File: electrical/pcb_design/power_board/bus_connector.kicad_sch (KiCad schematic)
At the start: 7 parts, among them J601 Interconnect_Power_CPU-Power_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, J603 Interconnect_Battery_Power-Po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

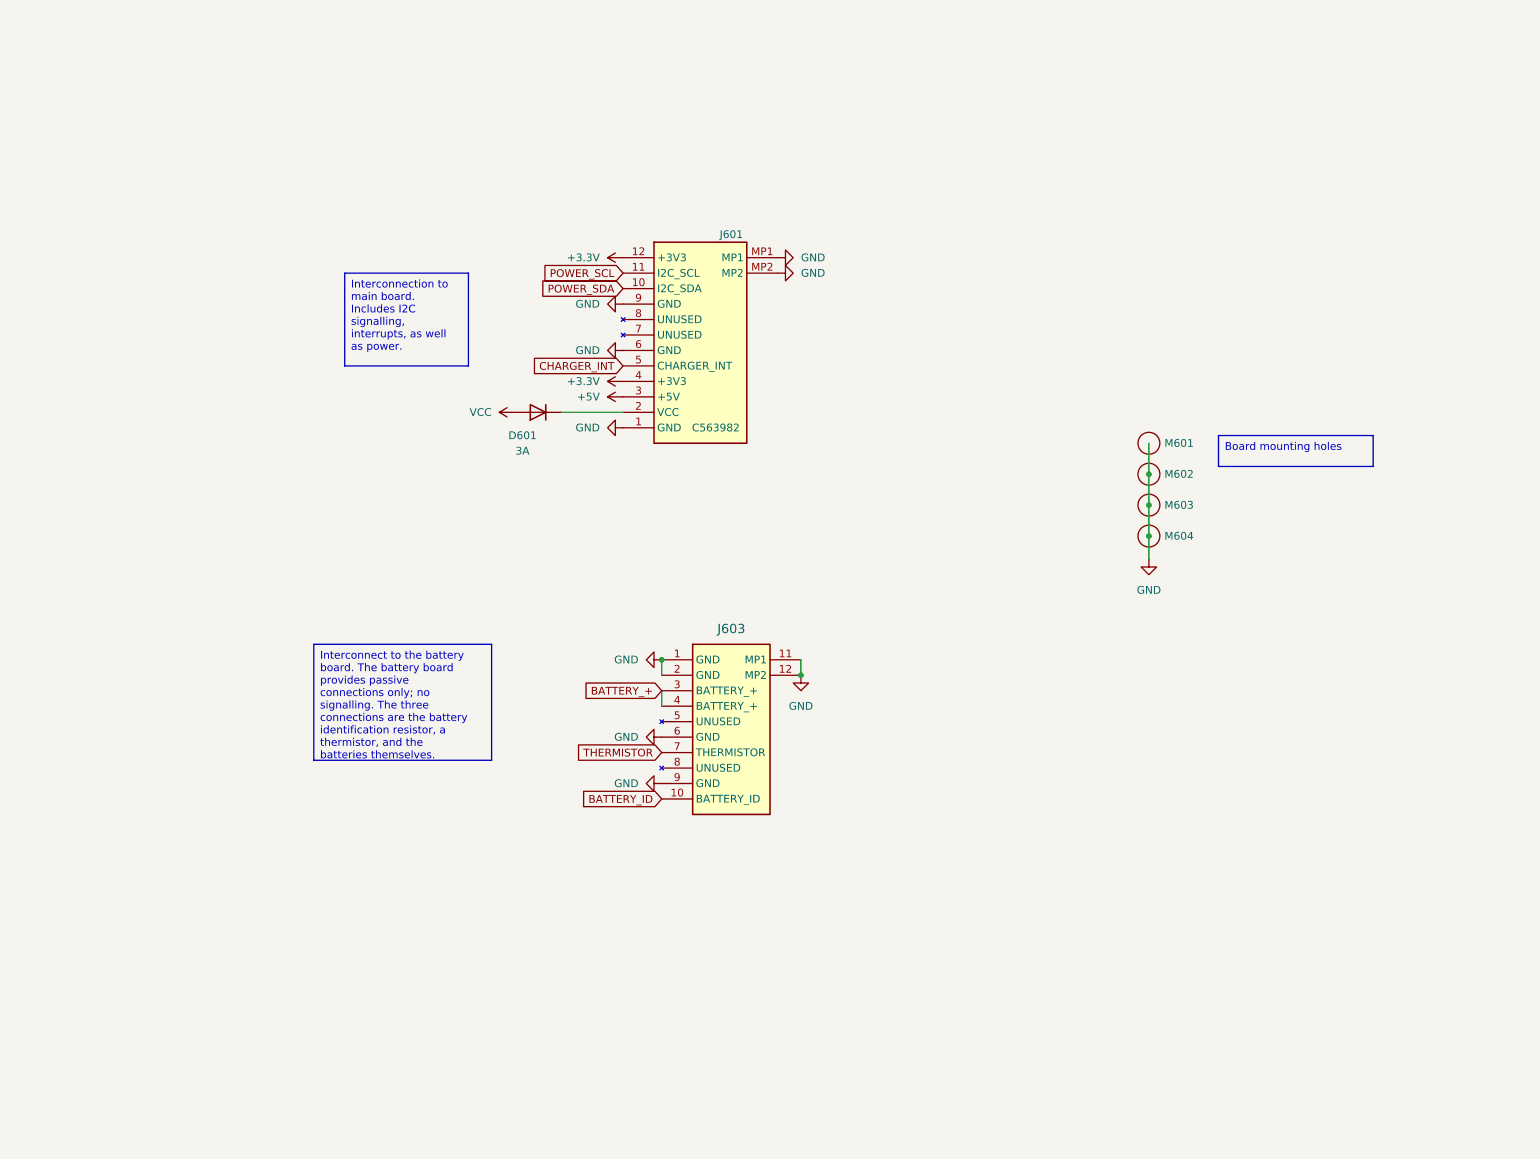
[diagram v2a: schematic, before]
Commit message: Sketched in PCB edge connectors
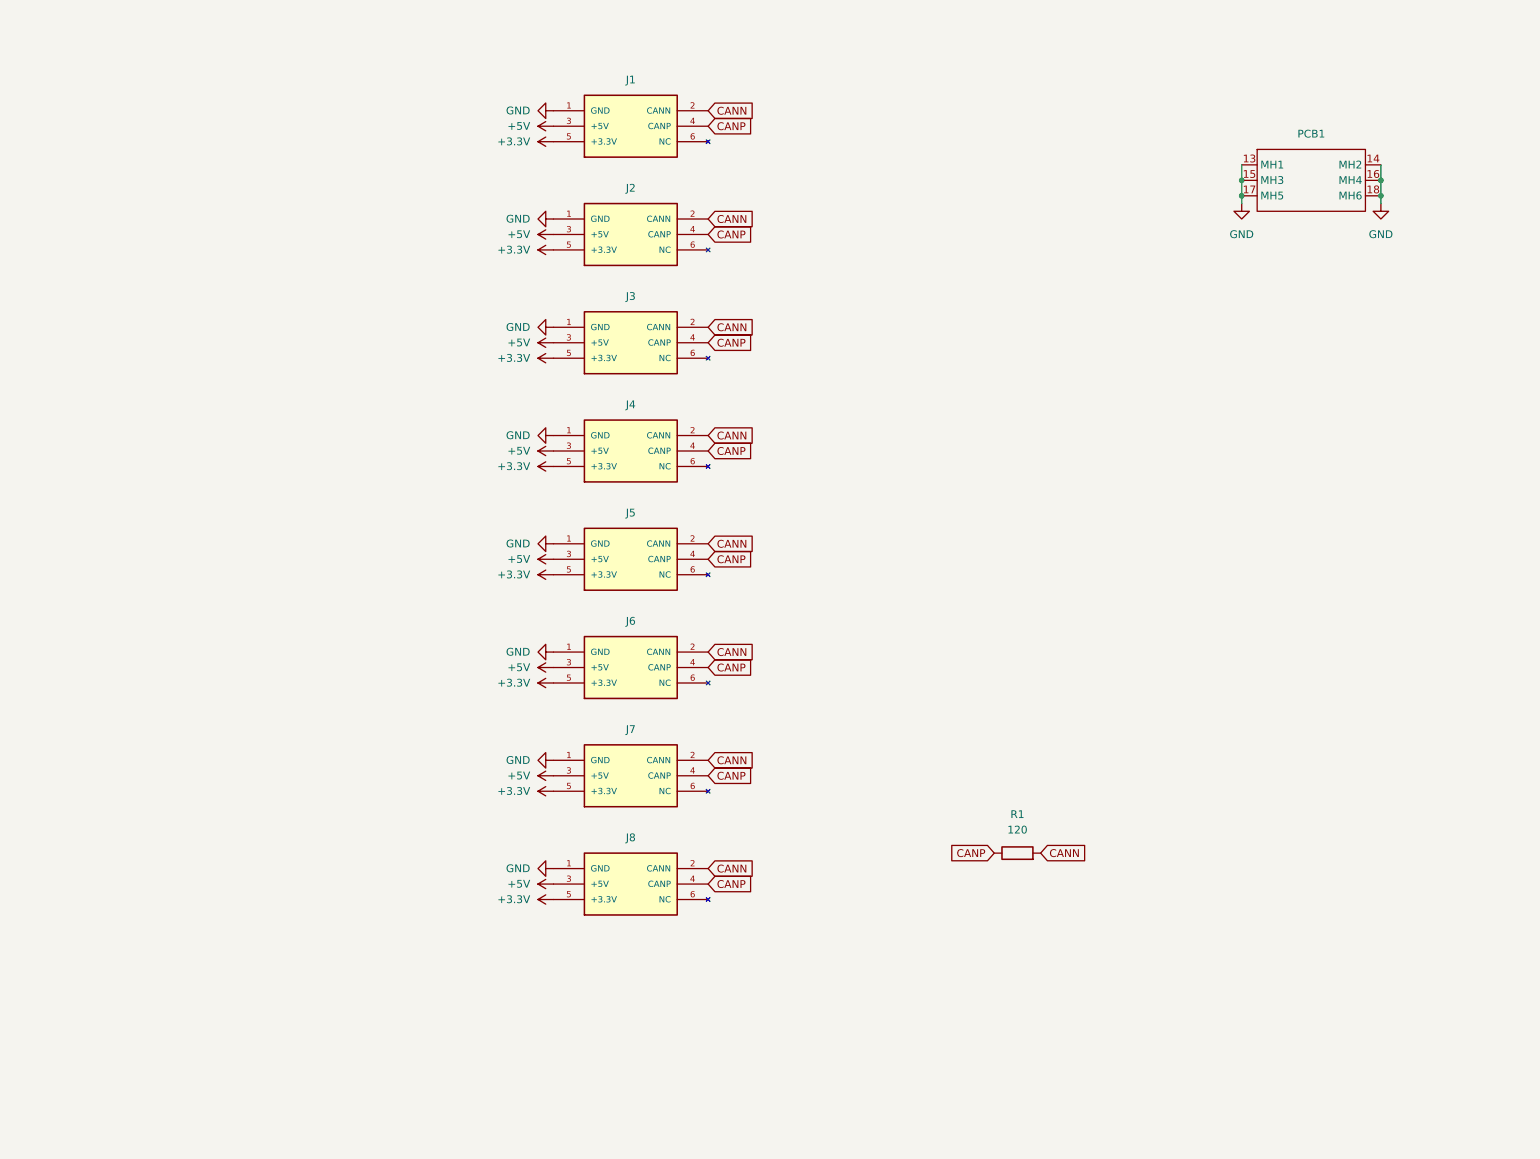
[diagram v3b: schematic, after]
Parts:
- removed D601: 3A, Diode_SMD:D_SOD-323, symbol Diode:1N4001
- removed J601: Interconnect_Power_CPU-Power_side, footprints:5040501291, symbol TVSC:Interconnect_Power_CPU-Power_side
- removed J603: Interconnect_Battery_Power-Power_side, footprints:504050-1091, symbol TVSC:Interconnect_Battery_Power-Power_side
- removed M601, M602, M603, M604: ~, MountingHole:MountingHole_3.2mm_M3_ISO7380_Pad_TopBottom, symbol mounting:Mounting_Hole_M3_ISO_7380
- added J1, J2, J3, J4, J5, J6, J7, J8: TE_Connectivity_7-5530843-7, footprints:TE_Connectivity_7-5530843-7, symbol TVSC:Backplane_Connector_Reversed
- added PCB1: ~, footprints:Interior_Side_Panel_PCB_Shape, symbol TVSC:Interior_Side_Panel_PCB
- added R1: 120, symbol Device:R
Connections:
- net +3.3V: now also J1.5 (+3.3V), J2.5 (+3.3V), J3.5 (+3.3V), J4.5 (+3.3V), J5.5 (+3.3V), J6.5 (+3.3V), J7.5 (+3.3V), J8.5 (+3.3V)
- net +5V: now also J1.3 (+5V), J2.3 (+5V), J3.3 (+5V), J4.3 (+5V), J5.3 (+5V), J6.3 (+5V), J7.3 (+5V), J8.3 (+5V)
- net GND: now also J1.1 (GND), J2.1 (GND), J3.1 (GND), J4.1 (GND), J5.1 (GND), J6.1 (GND), J7.1 (GND), J8.1 (GND), PCB1.13 (MH1), PCB1.14 (MH2), PCB1.15 (MH3), PCB1.16 (MH4), PCB1.17 (MH5), PCB1.18 (MH6)
- new net CANN: J1.2 (CANN), J2.2 (CANN), J3.2 (CANN), J4.2 (CANN), J5.2 (CANN), J6.2 (CANN), J7.2 (CANN), J8.2 (CANN), R1.2
- new net CANP: J1.4 (CANP), J2.4 (CANP), J3.4 (CANP), J4.4 (CANP), J5.4 (CANP), J6.4 (CANP), J7.4 (CANP), J8.4 (CANP), R1.1

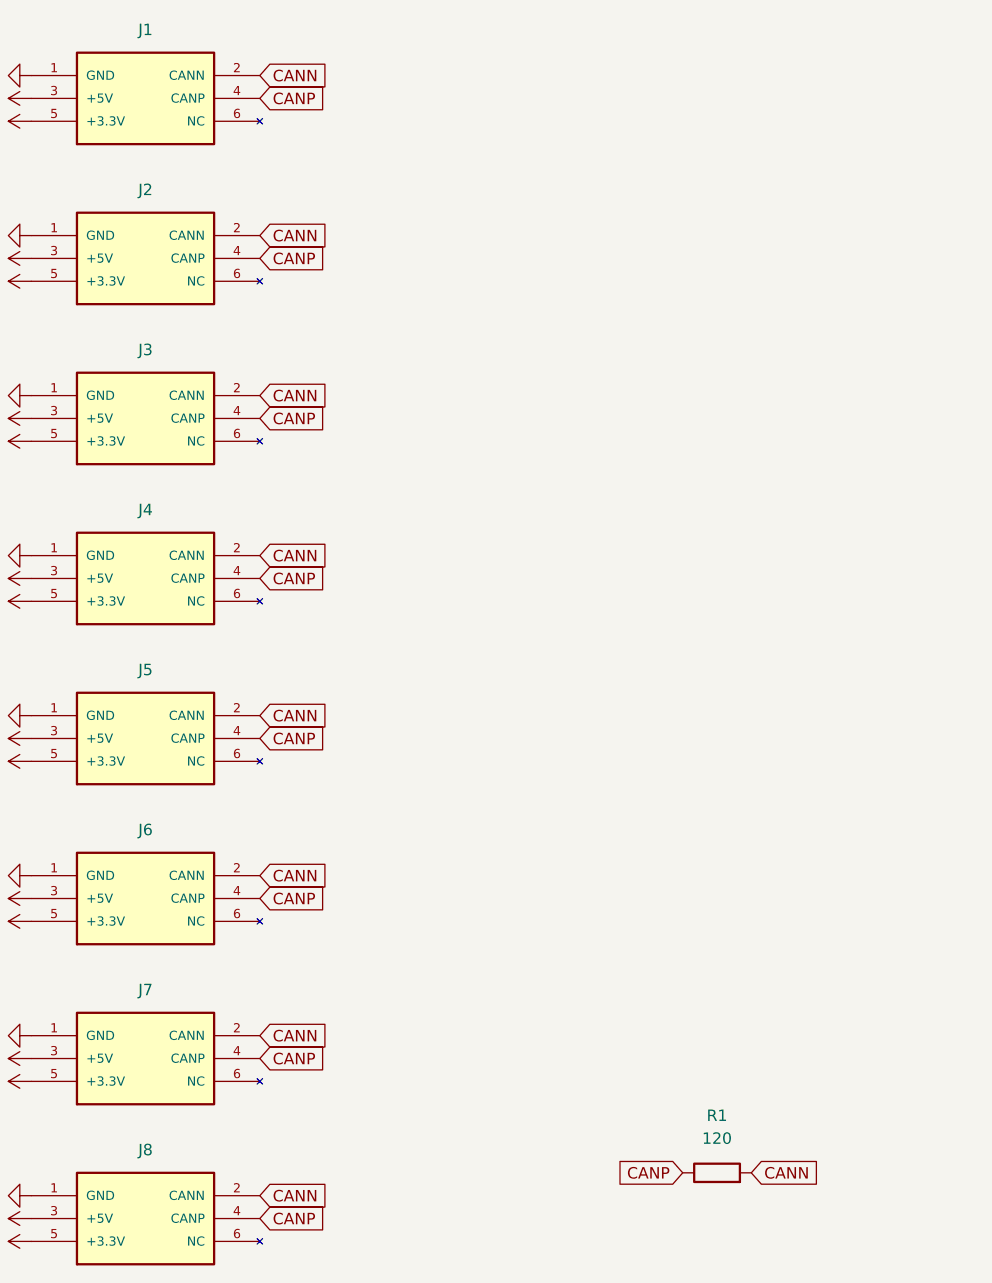
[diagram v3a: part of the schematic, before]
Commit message: Renamed CANP and CANN to CANH and CANL to follow standard conventions
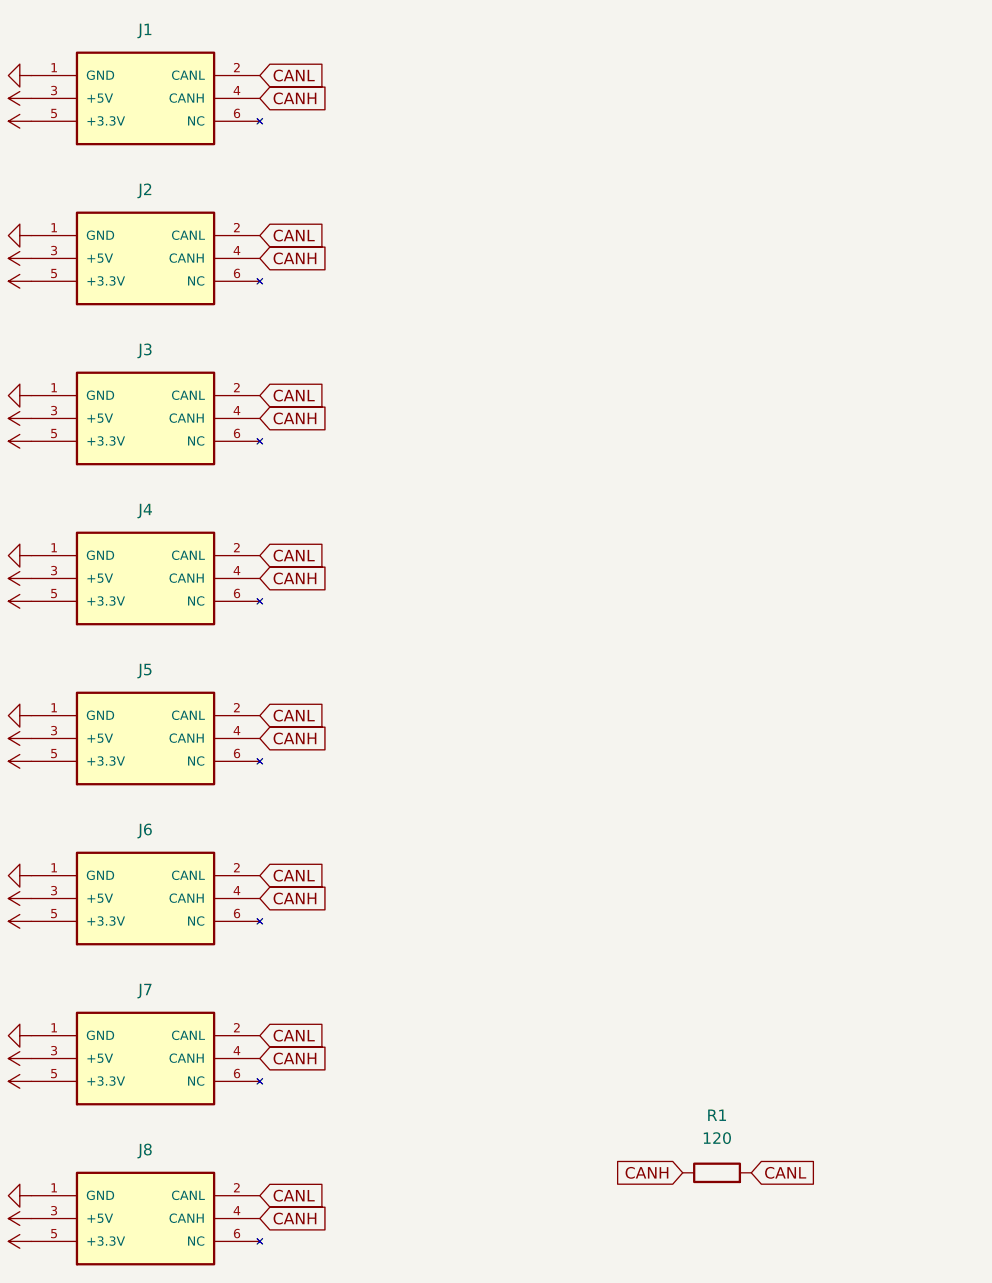
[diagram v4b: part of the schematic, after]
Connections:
- net CANN renamed CANL
- net CANP renamed CANH
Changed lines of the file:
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@@
     (stroke (width 0) (type default))
   )
-  (global_label "CANP" (shape input) (at 129.54 86.36 0) (fields_autoplaced)
+  (global_label "CANH" (shape input) (at 129.54 86.36 0) (fields_autoplaced)
     (effects (font (size 1.27 1.27)) (justify left))
     (property "Intersheetrefs" "${INTERSHEET_REFS}" (at 137.4843 86.36 0)
@@
     )
   )
-  (global_label "CANN" (shape input) (at 129.54 119.38 0) (fields_autoplaced)
+  (global_label "CANL" (shape input) (at 129.54 119.38 0) (fields_autoplaced)
     (effects (font (size 1.27 1.27)) (justify left))
     (property "Intersheetrefs" "${INTERSHEET_REFS}" (at 137.5448 119.38 0)
@@
     )
   )
-  (global_label "CANP" (shape input) (at 129.54 68.58 0) (fields_autoplaced)
+  (global_label "CANH" (shape input) (at 129.54 68.58 0) (fields_autoplaced)
     (effects (font (size 1.27 1.27)) (justify left))
     (property "Intersheetrefs" "${INTERSHEET_REFS}" (at 137.4843 68.58 0)
@@
     )
   )
-  (global_label "CANN" (shape input) (at 129.54 154.94 0) (fields_autoplaced)
+  (global_label "CANL" (shape input) (at 129.54 154.94 0) (fields_autoplaced)
     (effects (font (size 1.27 1.27)) (justify left))
     (property "Intersheetrefs" "${INTERSHEET_REFS}" (at 137.5448 154.94 0)
@@
     )
   )
-  (global_label "CANP" (shape input) (at 129.54 33.02 0) (fields_autoplaced)
+  (global_label "CANH" (shape input) (at 129.54 33.02 0) (fields_autoplaced)
     (effects (font (size 1.27 1.27)) (justify left))
     (property "Intersheetrefs" "${INTERSHEET_REFS}" (at 137.4843 33.02 0)
@@
     )
   )
-  (global_label "CANN" (shape input) (at 129.54 66.04 0) (fields_autoplaced)
+  (global_label "CANL" (shape input) (at 129.54 66.04 0) (fields_autoplaced)
     (effects (font (size 1.27 1.27)) (justify left))
     (property "Intersheetrefs" "${INTERSHEET_REFS}" (at 137.5448 66.04 0)
@@
     )
   )
-  (global_label "CANP" (shape input) (at 129.54 121.92 0) (fields_autoplaced)
+  (global_label "CANH" (shape input) (at 129.54 121.92 0) (fields_autoplaced)
     (effects (font (size 1.27 1.27)) (justify left))
     (property "Intersheetrefs" "${INTERSHEET_REFS}" (at 137.4843 121.92 0)
@@
     )
   )
-  (global_label "CANP" (shape input) (at 176.53 152.4 180) (fields_autoplaced)
+  (global_label "CANH" (shape input) (at 176.53 152.4 180) (fields_autoplaced)
     (effects (font (size 1.27 1.27)) (justify right))
     (property "Intersheetrefs" "${INTERSHEET_REFS}" (at 168.5857 152.4 0)
@@
     )
   )
-  (global_label "CANN" (shape input) (at 129.54 30.48 0) (fields_autoplaced)
+  (global_label "CANL" (shape input) (at 129.54 30.48 0) (fields_autoplaced)
     (effects (font (size 1.27 1.27)) (justify left))
     (property "Intersheetrefs" "${INTERSHEET_REFS}" (at 137.5448 30.48 0)
@@
     )
   )
-  (global_label "CANN" (shape input) (at 129.54 101.6 0) (fields_autoplaced)
+  (global_label "CANL" (shape input) (at 129.54 101.6 0) (fields_autoplaced)
     (effects (font (size 1.27 1.27)) (justify left))
     (property "Intersheetrefs" "${INTERSHEET_REFS}" (at 137.5448 101.6 0)
@@
     )
   )
-  (global_label "CANP" (shape input) (at 129.54 157.48 0) (fields_autoplaced)
+  (global_label "CANH" (shape input) (at 129.54 157.48 0) (fields_autoplaced)
     (effects (font (size 1.27 1.27)) (justify left))
     (property "Intersheetrefs" "${INTERSHEET_REFS}" (at 137.4843 157.48 0)
@@
     )
   )
-  (global_label "CANP" (shape input) (at 129.54 104.14 0) (fields_autoplaced)
+  (global_label "CANH" (shape input) (at 129.54 104.14 0) (fields_autoplaced)
     (effects (font (size 1.27 1.27)) (justify left))
     (property "Intersheetrefs" "${INTERSHEET_REFS}" (at 137.4843 104.14 0)
@@
     )
   )
-  (global_label "CANP" (shape input) (at 129.54 139.7 0) (fields_autoplaced)
+  (global_label "CANH" (shape input) (at 129.54 139.7 0) (fields_autoplaced)
     (effects (font (size 1.27 1.27)) (justify left))
     (property "Intersheetrefs" "${INTERSHEET_REFS}" (at 137.4843 139.7 0)
@@
     )
   )
-  (global_label "CANN" (shape input) (at 129.54 83.82 0) (fields_autoplaced)
+  (global_label "CANL" (shape input) (at 129.54 83.82 0) (fields_autoplaced)
     (effects (font (size 1.27 1.27)) (justify left))
     (property "Intersheetrefs" "${INTERSHEET_REFS}" (at 137.5448 83.82 0)
@@
     )
   )
-  (global_label "CANN" (shape input) (at 184.15 152.4 0) (fields_autoplaced)
+  (global_label "CANL" (shape input) (at 184.15 152.4 0) (fields_autoplaced)
     (effects (font (size 1.27 1.27)) (justify left))
     (property "Intersheetrefs" "${INTERSHEET_REFS}" (at 192.1548 152.4 0)
@@
     )
   )
-  (global_label "CANN" (shape input) (at 129.54 48.26 0) (fields_autoplaced)
+  (global_label "CANL" (shape input) (at 129.54 48.26 0) (fields_autoplaced)
     (effects (font (size 1.27 1.27)) (justify left))
     (property "Intersheetrefs" "${INTERSHEET_REFS}" (at 137.5448 48.26 0)
@@
     )
   )
-  (global_label "CANN" (shape input) (at 129.54 137.16 0) (fields_autoplaced)
+  (global_label "CANL" (shape input) (at 129.54 137.16 0) (fields_autoplaced)
     (effects (font (size 1.27 1.27)) (justify left))
     (property "Intersheetrefs" "${INTERSHEET_REFS}" (at 137.5448 137.16 0)
@@
     )
   )
-  (global_label "CANP" (shape input) (at 129.54 50.8 0) (fields_autoplaced)
+  (global_label "CANH" (shape input) (at 129.54 50.8 0) (fields_autoplaced)
     (effects (font (size 1.27 1.27)) (justify left))
     (property "Intersheetrefs" "${INTERSHEET_REFS}" (at 137.4843 50.8 0)
